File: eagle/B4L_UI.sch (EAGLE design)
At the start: 57 parts, among them Q1 STP40NF03L, Q2 STP40NF03L

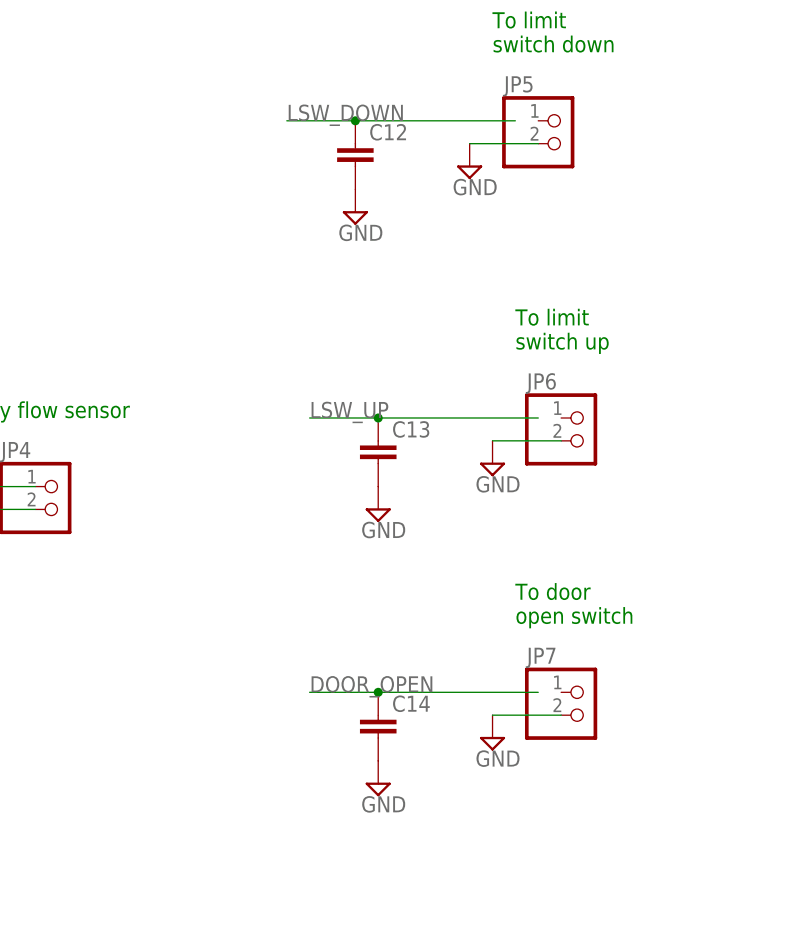
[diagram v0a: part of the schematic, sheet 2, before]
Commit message: Add value for capacitors
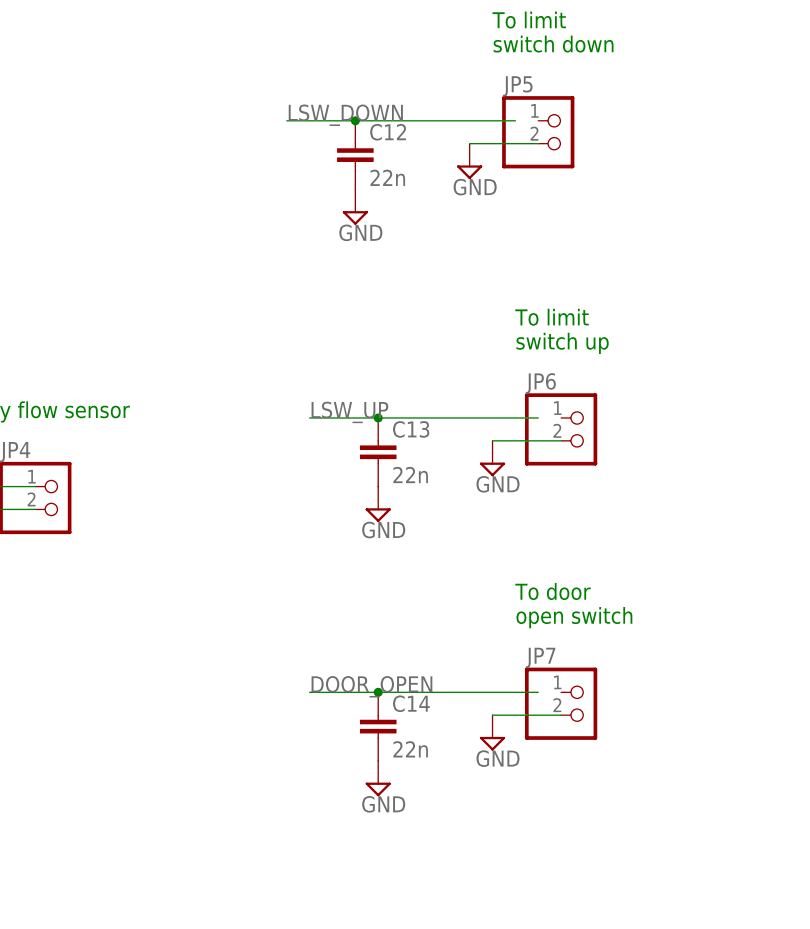
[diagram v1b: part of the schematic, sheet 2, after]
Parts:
- C12, C13, C14: value (none) -> 22n
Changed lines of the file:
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@@
 <part name="SUPPLY23" library="supply2" library_urn="urn:adsk.eagle:library:372" deviceset="GND" device=""/>
 <part name="JP5" library="pinhead" library_urn="urn:adsk.eagle:library:325" deviceset="PINHD-1X2" device="" package3d_urn="urn:adsk.eagle:package:22435/2"/>
-<part name="C12" library="capacitor-wima" library_urn="urn:adsk.eagle:library:116" deviceset="C" device="2,5-3" package3d_urn="urn:adsk.eagle:package:5436/1"/>
+<part name="C12" library="capacitor-wima" library_urn="urn:adsk.eagle:library:116" deviceset="C" device="2,5-3" package3d_urn="urn:adsk.eagle:package:5436/1" value="22n"/>
 <part name="SUPPLY24" library="supply2" library_urn="urn:adsk.eagle:library:372" deviceset="GND" device=""/>
 <part name="SUPPLY25" library="supply2" library_urn="urn:adsk.eagle:library:372" deviceset="GND" device=""/>
 <part name="JP6" library="pinhead" library_urn="urn:adsk.eagle:library:325" deviceset="PINHD-1X2" device="" package3d_urn="urn:adsk.eagle:package:22435/2"/>
-<part name="C13" library="capacitor-wima" library_urn="urn:adsk.eagle:library:116" deviceset="C" device="2,5-3" package3d_urn="urn:adsk.eagle:package:5436/1"/>
+<part name="C13" library="capacitor-wima" library_urn="urn:adsk.eagle:library:116" deviceset="C" device="2,5-3" package3d_urn="urn:adsk.eagle:package:5436/1" value="22n"/>
 <part name="SUPPLY26" library="supply2" library_urn="urn:adsk.eagle:library:372" deviceset="GND" device=""/>
 <part name="SUPPLY27" library="supply2" library_urn="urn:adsk.eagle:library:372" deviceset="GND" device=""/>
 <part name="JP7" library="pinhead" library_urn="urn:adsk.eagle:library:325" deviceset="PINHD-1X2" device="" package3d_urn="urn:adsk.eagle:package:22435/2"/>
-<part name="C14" library="capacitor-wima" library_urn="urn:adsk.eagle:library:116" deviceset="C" device="2,5-3" package3d_urn="urn:adsk.eagle:package:5436/1"/>
+<part name="C14" library="capacitor-wima" library_urn="urn:adsk.eagle:library:116" deviceset="C" device="2,5-3" package3d_urn="urn:adsk.eagle:package:5436/1" value="22n"/>
 <part name="SUPPLY28" library="supply2" library_urn="urn:adsk.eagle:library:372" deviceset="GND" device=""/>
 <part name="SUPPLY29" library="supply2" library_urn="urn:adsk.eagle:library:372" deviceset="GND" device=""/>

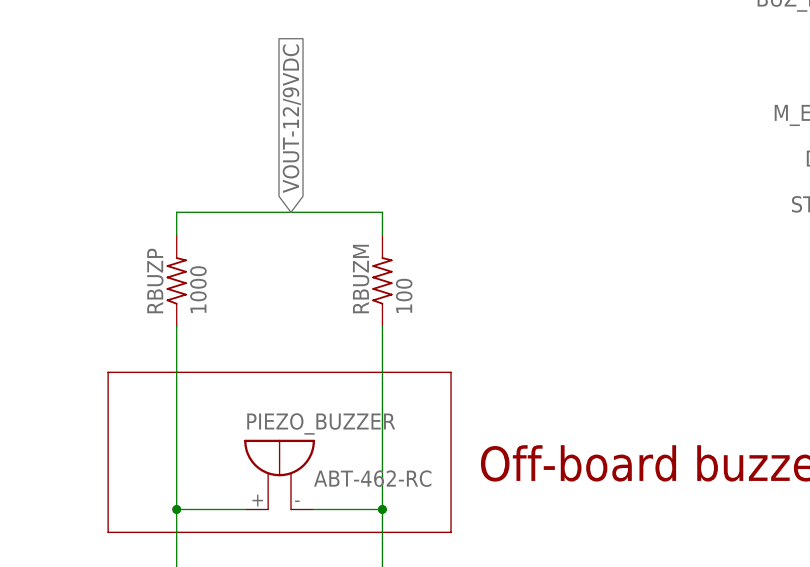
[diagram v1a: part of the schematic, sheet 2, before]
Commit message: [UI board] Correction of RBUZM resistor value
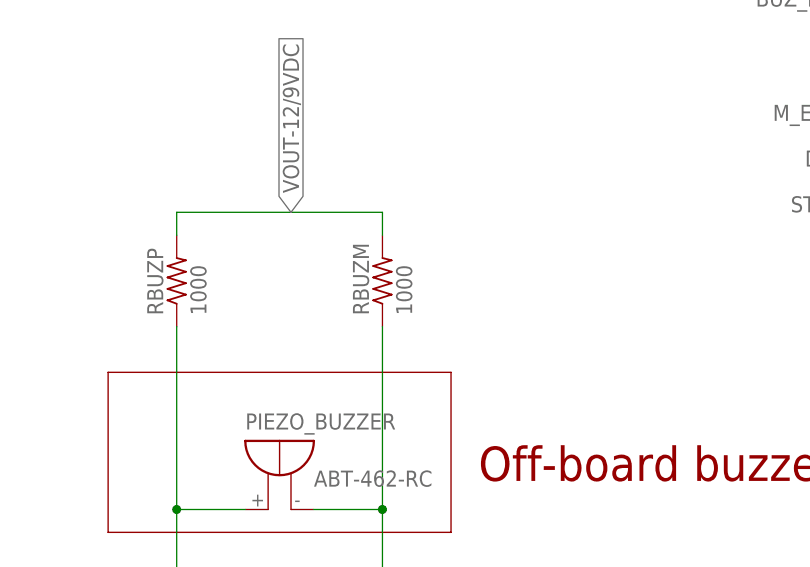
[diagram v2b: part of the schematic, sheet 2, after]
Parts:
- RBUZM: value 100 -> 1000
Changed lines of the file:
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@@
 <?xml version="1.0" encoding="utf-8"?>
 <!DOCTYPE eagle SYSTEM "eagle.dtd">
-<eagle version="9.6.1">
+<eagle version="9.2.2">
 <drawing>
 <settings>
@@
 <part name="SUPPLY22" library="supply2" library_urn="urn:adsk.eagle:library:372" deviceset="GND" device=""/>
 <part name="RBUZP" library="rcl" library_urn="urn:adsk.eagle:library:334" deviceset="R-US_" device="0309/12" package3d_urn="urn:adsk.eagle:package:23571/1" value="1000"/>
-<part name="RBUZM" library="rcl" library_urn="urn:adsk.eagle:library:334" deviceset="R-US_" device="0309/12" package3d_urn="urn:adsk.eagle:package:23571/1" value="100"/>
+<part name="RBUZM" library="rcl" library_urn="urn:adsk.eagle:library:334" deviceset="R-US_" device="0309/12" package3d_urn="urn:adsk.eagle:package:23571/1" value="1000"/>
 <part name="PIEZO_BUZZER" library="buzzer" library_urn="urn:adsk.eagle:library:113" deviceset="F/TMB" device="" package3d_urn="urn:adsk.eagle:package:5260/1" value="ABT-462-RC"/>
 <part name="JP2" library="pinhead" library_urn="urn:adsk.eagle:library:325" deviceset="PINHD-1X6" device="" package3d_urn="urn:adsk.eagle:package:22472/2"/>

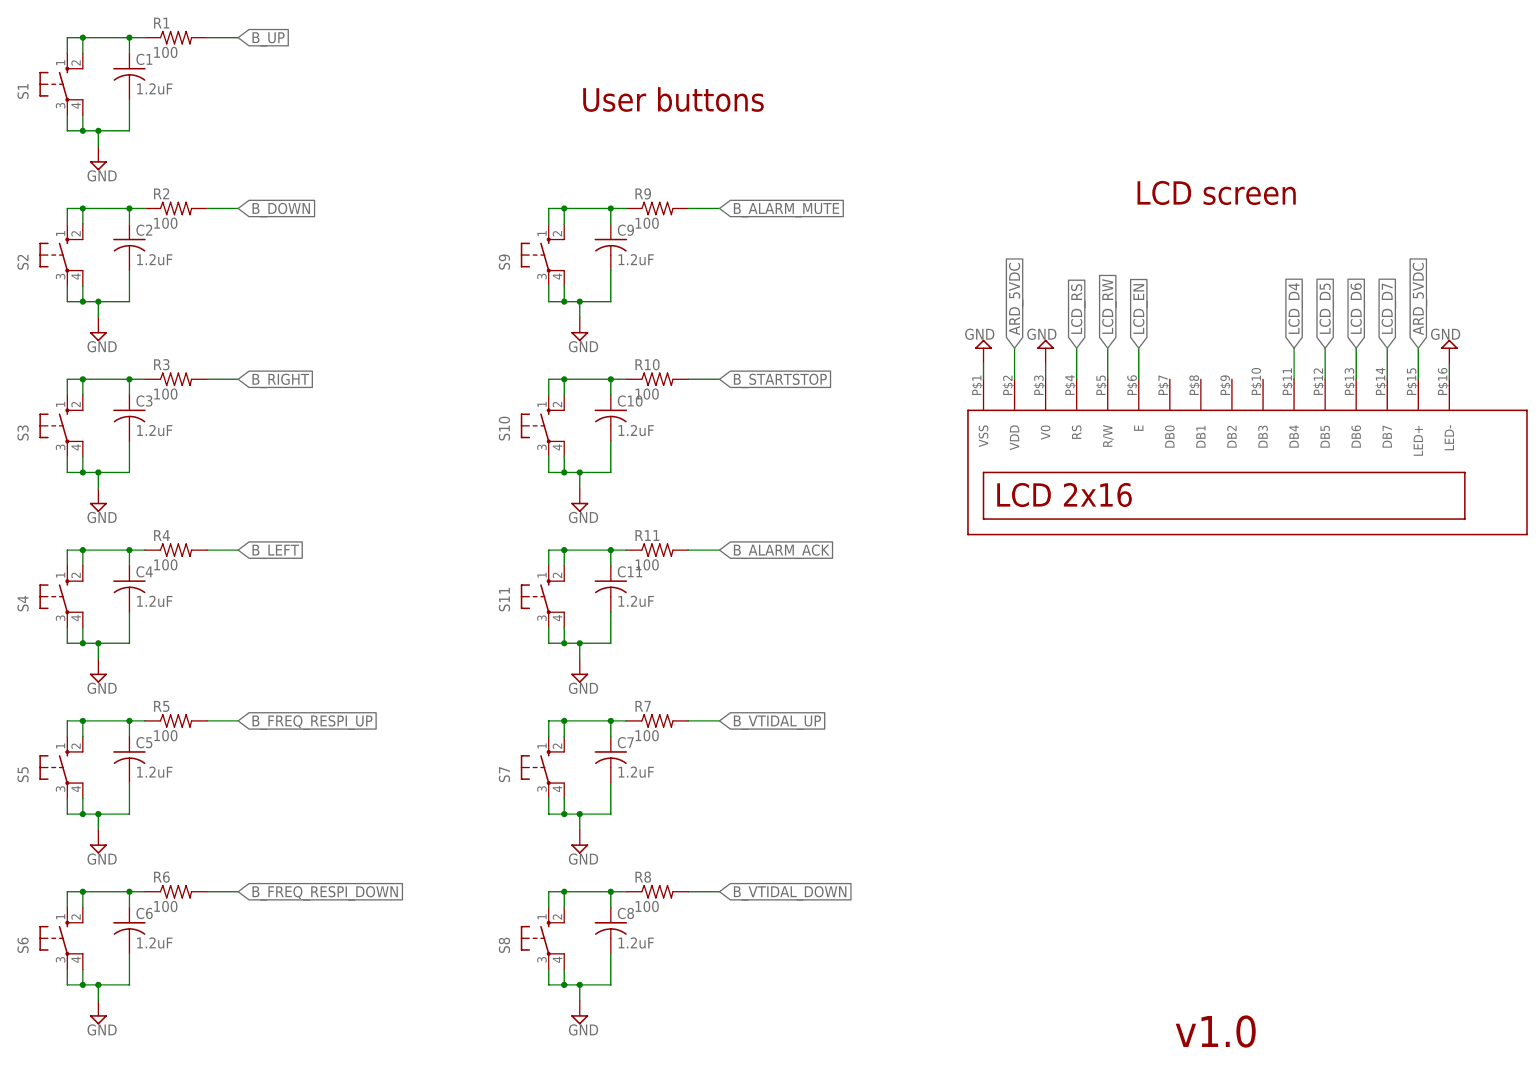
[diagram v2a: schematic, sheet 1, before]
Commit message: [UI board] Correction of capacitors placement near the buttons
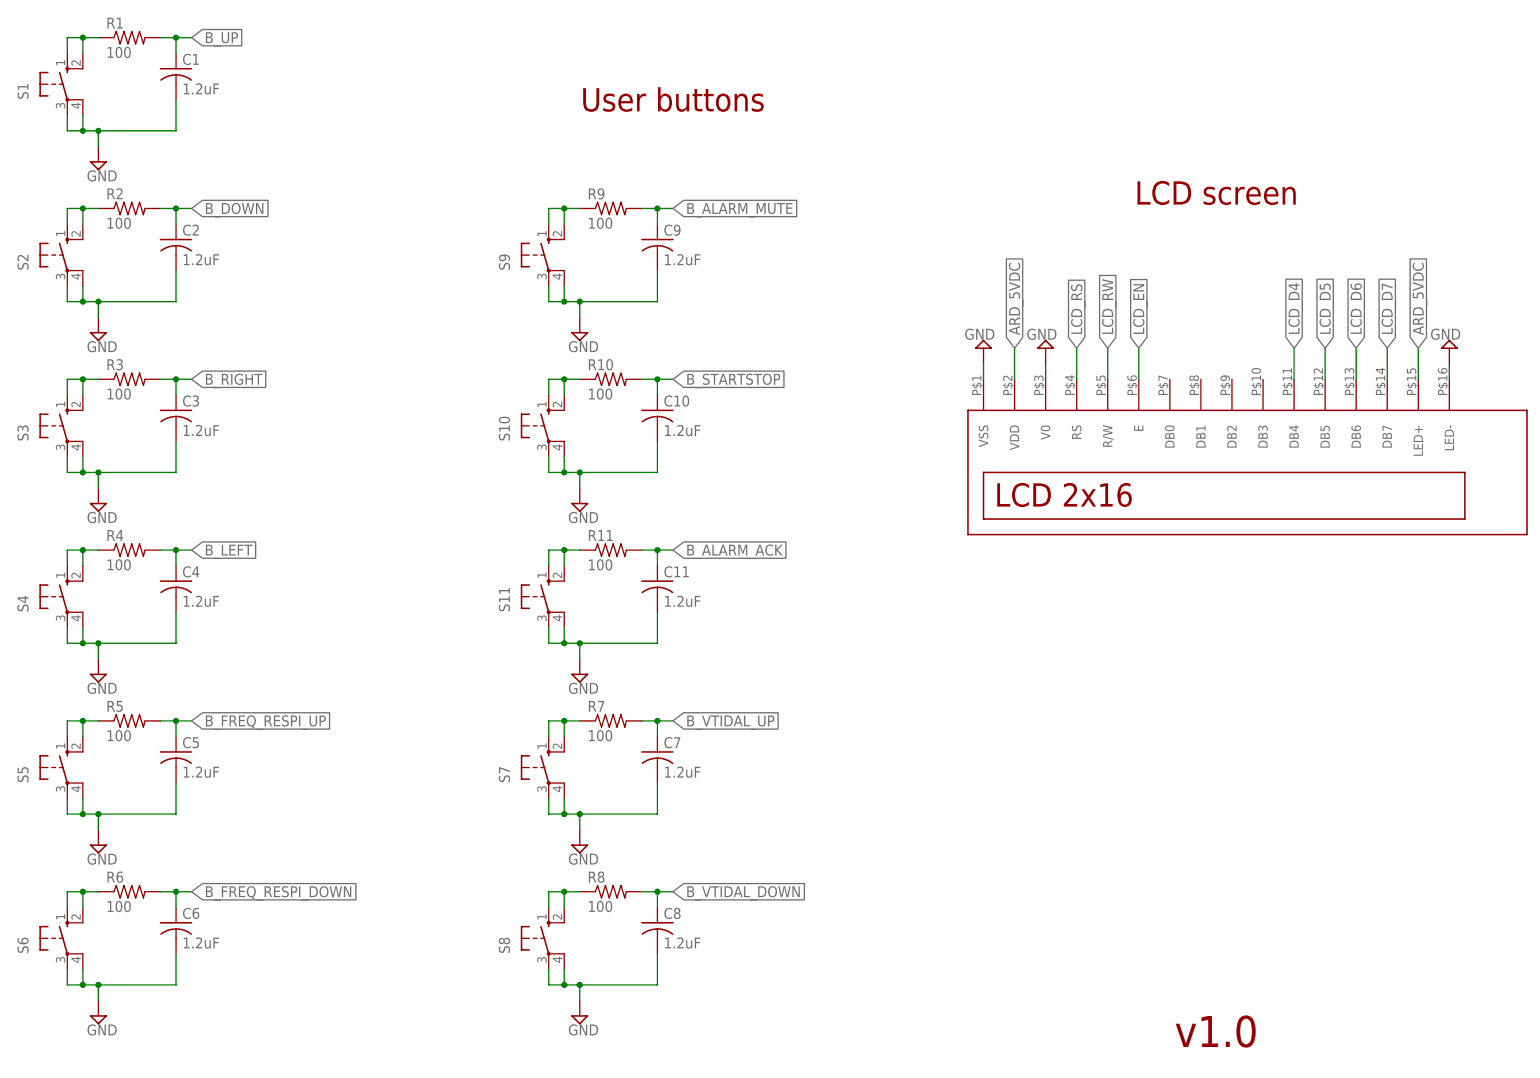
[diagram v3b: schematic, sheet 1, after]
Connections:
- net B_ALARM_ACK: now also C11.1
- net B_ALARM_MUTE: now also C9.1
- net B_DOWN: now also C2.1
- net B_FREQ_RESPI_DOWN: now also C6.1
- net B_FREQ_RESPI_UP: now also C5.1
- net B_LEFT: now also C4.1
- net B_RIGHT: now also C3.1
- net B_STARTSTOP: now also C10.1
- net B_UP: now also C1.1
- net B_VTIDAL_DOWN: now also C8.1
- net B_VTIDAL_UP: now also C7.1
- net N$1: no longer C1.1
- net N$10: no longer C11.1
- net N$11: no longer C9.1
- net N$13: no longer C10.1
- net N$15: no longer C8.1
- net N$17: no longer C7.1
- net N$19: no longer C6.1
- net N$3: no longer C2.1
- net N$5: no longer C3.1
- net N$7: no longer C4.1
- net N$9: no longer C5.1
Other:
- moved on the sheet: C1, C10, C11, C2, C3, C4, C5, C6, C7, C8, C9, R1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
